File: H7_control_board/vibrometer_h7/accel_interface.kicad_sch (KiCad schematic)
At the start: 9 parts

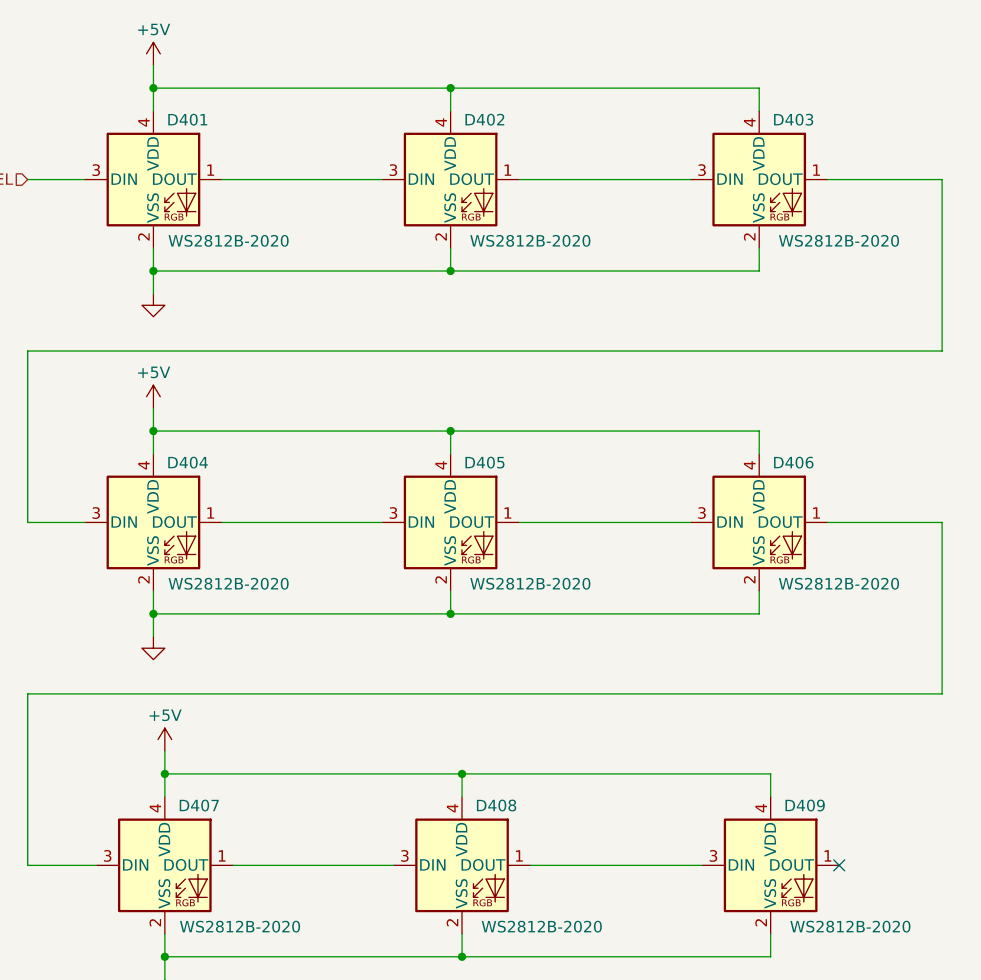
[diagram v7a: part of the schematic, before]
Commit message: updated reference designator naming
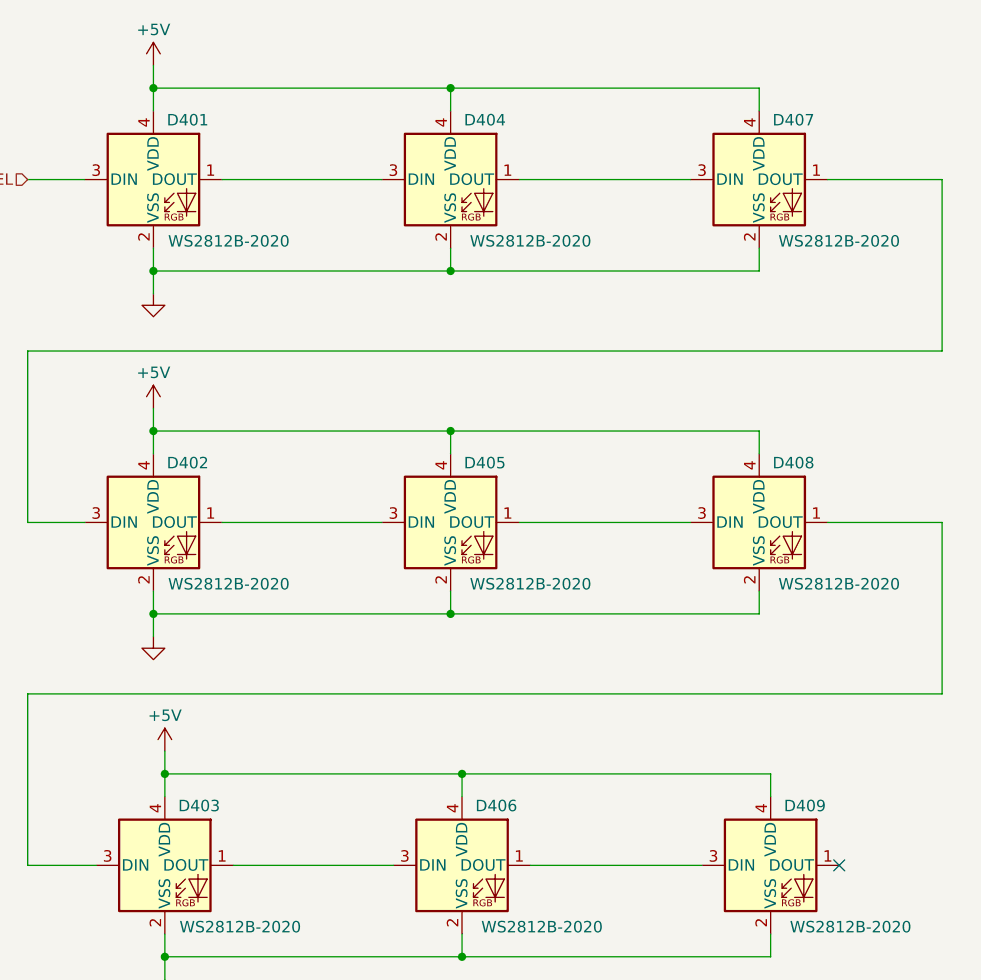
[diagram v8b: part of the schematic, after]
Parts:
- renumbered D404 to D402, D407 to D403, D402 to D404, D408 to D406, D403 to D407, D406 to D408
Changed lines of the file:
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@@
 		(on_board yes)
 		(dnp no)
-		(property "Reference" "#PWR031"
+		(property "Reference" "#PWR0407"
 			(at 185.42 41.91 0)
 			(effects
@@
 			(project "vibrometer_h7"
 				(path "/18de6987-156a-4b34-871e-cbbe1d261986/719d72ab-d813-461f-9482-52ce573716fd"
-					(reference "#PWR031")
+					(reference "#PWR0407")
 					(unit 1)
 				)
@@
 		(on_board yes)
 		(dnp no)
-		(property "Reference" "D402"
+		(property "Reference" "D404"
 			(at 100.33 44.196 0)
 			(effects
@@
 			(project "vibrometer_h7"
 				(path "/18de6987-156a-4b34-871e-cbbe1d261986/719d72ab-d813-461f-9482-52ce573716fd"
-					(reference "D402")
+					(reference "D404")
 					(unit 1)
 				)
@@
 		(on_board yes)
 		(dnp no)
-		(property "Reference" "D406"
+		(property "Reference" "D408"
 			(at 134.62 82.296 0)
 			(effects
@@
 			(project "vibrometer_h7"
 				(path "/18de6987-156a-4b34-871e-cbbe1d261986/719d72ab-d813-461f-9482-52ce573716fd"
-					(reference "D406")
+					(reference "D408")
 					(unit 1)
 				)
@@
 		(on_board yes)
 		(dnp no)
-		(property "Reference" "#PWR032"
+		(property "Reference" "#PWR0408"
 			(at 185.42 67.31 0)
 			(effects
@@
 			(project "vibrometer_h7"
 				(path "/18de6987-156a-4b34-871e-cbbe1d261986/719d72ab-d813-461f-9482-52ce573716fd"
-					(reference "#PWR032")
+					(reference "#PWR0408")
 					(unit 1)
 				)
@@
 		(on_board yes)
 		(dnp no)
-		(property "Reference" "#PWR035"
+		(property "Reference" "#PWR0411"
 			(at 185.42 118.11 0)
 			(effects
@@
 			(project "vibrometer_h7"
 				(path "/18de6987-156a-4b34-871e-cbbe1d261986/719d72ab-d813-461f-9482-52ce573716fd"
-					(reference "#PWR035")
+					(reference "#PWR0411")
 					(unit 1)
 				)
@@
 		(on_board yes)
 		(dnp no)
-		(property "Reference" "#PWR056"
+		(property "Reference" "#PWR0403"
 			(at 63.5 80.01 0)
 			(effects
@@
 			(project "vibrometer_h7"
 				(path "/18de6987-156a-4b34-871e-cbbe1d261986/719d72ab-d813-461f-9482-52ce573716fd"
-					(reference "#PWR056")
+					(reference "#PWR0403")
 					(unit 1)
 				)
@@
 		(dnp no)
 		(fields_autoplaced yes)
-		(property "Reference" "#PWR057"
+		(property "Reference" "#PWR0404"
 			(at 63.5 107.95 0)
 			(effects
@@
 			(project "vibrometer_h7"
 				(path "/18de6987-156a-4b34-871e-cbbe1d261986/719d72ab-d813-461f-9482-52ce573716fd"
-					(reference "#PWR057")
+					(reference "#PWR0404")
 					(unit 1)
 				)
@@
 		(on_board yes)
 		(dnp no)
-		(property "Reference" "#PWR058"
+		(property "Reference" "#PWR0405"
 			(at 64.77 118.11 0)
 			(effects
@@
 			(project "vibrometer_h7"
 				(path "/18de6987-156a-4b34-871e-cbbe1d261986/719d72ab-d813-461f-9482-52ce573716fd"
-					(reference "#PWR058")
+					(reference "#PWR0405")
 					(unit 1)
 				)
@@
 		(on_board yes)
 		(dnp no)
-		(property "Reference" "D408"
+		(property "Reference" "D406"
 			(at 101.6 120.396 0)
 			(effects
@@
 			(project "vibrometer_h7"
 				(path "/18de6987-156a-4b34-871e-cbbe1d261986/719d72ab-d813-461f-9482-52ce573716fd"
-					(reference "D408")
+					(reference "D406")
 					(unit 1)
 				)
@@
 		(on_board yes)
 		(dnp no)
-		(property "Reference" "D403"
+		(property "Reference" "D407"
 			(at 134.62 44.196 0)
 			(effects
@@
 			(project "vibrometer_h7"
 				(path "/18de6987-156a-4b34-871e-cbbe1d261986/719d72ab-d813-461f-9482-52ce573716fd"
-					(reference "D403")
+					(reference "D407")
 					(unit 1)
 				)
@@
 		(on_board yes)
 		(dnp no)
-		(property "Reference" "#PWR033"
+		(property "Reference" "#PWR0409"
 			(at 185.42 80.01 0)
 			(effects
@@
 			(project "vibrometer_h7"
 				(path "/18de6987-156a-4b34-871e-cbbe1d261986/719d72ab-d813-461f-9482-52ce573716fd"
-					(reference "#PWR033")
+					(reference "#PWR0409")
 					(unit 1)
 				)
@@
 		(on_board yes)
 		(dnp no)
-		(property "Reference" "#PWR038"
+		(property "Reference" "#PWR0412"
 			(at 185.42 143.51 0)
 			(effects
@@
 			(project "vibrometer_h7"
 				(path "/18de6987-156a-4b34-871e-cbbe1d261986/719d72ab-d813-461f-9482-52ce573716fd"
-					(reference "#PWR038")
+					(reference "#PWR0412")
 					(unit 1)
 				)
@@
 		(on_board yes)
 		(dnp no)
-		(property "Reference" "D407"
+		(property "Reference" "D403"
 			(at 68.58 120.396 0)
 			(effects
@@
 			(project "vibrometer_h7"
 				(path "/18de6987-156a-4b34-871e-cbbe1d261986/719d72ab-d813-461f-9482-52ce573716fd"
-					(reference "D407")
+					(reference "D403")
 					(unit 1)
 				)
@@
 		(dnp no)
 		(fields_autoplaced yes)
-		(property "Reference" "#PWR059"
+		(property "Reference" "#PWR0406"
 			(at 64.77 146.05 0)
 			(effects
@@
 			(project "vibrometer_h7"
 				(path "/18de6987-156a-4b34-871e-cbbe1d261986/719d72ab-d813-461f-9482-52ce573716fd"
-					(reference "#PWR059")
+					(reference "#PWR0406")
 					(unit 1)
 				)
@@
 		(dnp no)
 		(fields_autoplaced yes)
-		(property "Reference" "#PWR055"
+		(property "Reference" "#PWR0402"
 			(at 63.5 69.85 0)
 			(effects
@@
 			(project "vibrometer_h7"
 				(path "/18de6987-156a-4b34-871e-cbbe1d261986/719d72ab-d813-461f-9482-52ce573716fd"
-					(reference "#PWR055")
+					(reference "#PWR0402")
 					(unit 1)
 				)
@@
 		(on_board yes)
 		(dnp no)
-		(property "Reference" "#PWR054"
+		(property "Reference" "#PWR0401"
 			(at 63.5 41.91 0)
 			(effects
@@
 			(project "vibrometer_h7"
 				(path "/18de6987-156a-4b34-871e-cbbe1d261986/719d72ab-d813-461f-9482-52ce573716fd"
-					(reference "#PWR054")
+					(reference "#PWR0401")
 					(unit 1)
 				)
@@
 		(on_board yes)
 		(dnp no)
-		(property "Reference" "D404"
+		(property "Reference" "D402"
 			(at 67.31 82.296 0)
 			(effects
@@
 			(project "vibrometer_h7"
 				(path "/18de6987-156a-4b34-871e-cbbe1d261986/719d72ab-d813-461f-9482-52ce573716fd"
-					(reference "D404")
+					(reference "D402")
 					(unit 1)
 				)
@@
 		(on_board yes)
 		(dnp no)
-		(property "Reference" "#PWR034"
+		(property "Reference" "#PWR0410"
 			(at 185.42 105.41 0)
 			(effects
@@
 			(project "vibrometer_h7"
 				(path "/18de6987-156a-4b34-871e-cbbe1d261986/719d72ab-d813-461f-9482-52ce573716fd"
-					(reference "#PWR034")
-					(unit 1)
-				)
+					(reference "#PWR0410")
+					(unit 1)
+				)
